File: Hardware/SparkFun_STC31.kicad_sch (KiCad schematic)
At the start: 25 parts, among them J3 Qwiic_RA, J4 I2C, J5 Qwiic_RA, U1 VEML7700-TT

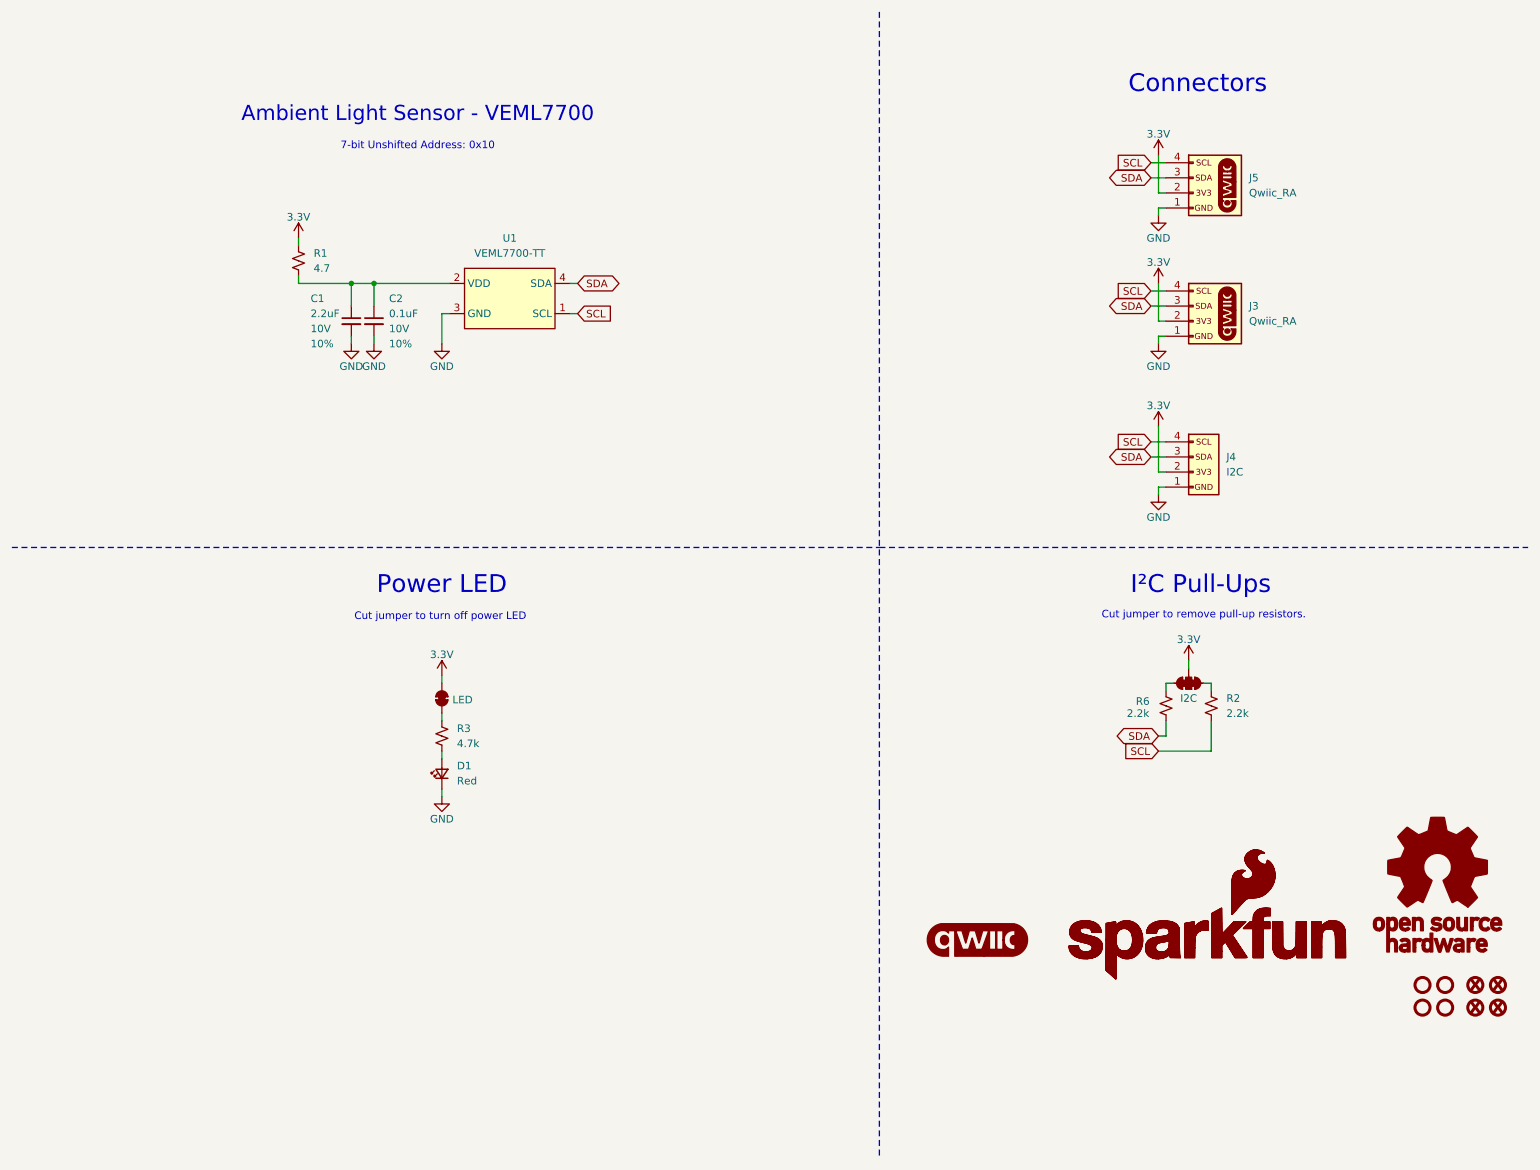
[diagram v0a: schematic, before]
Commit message: Updates the gitignore, finishes the schematic
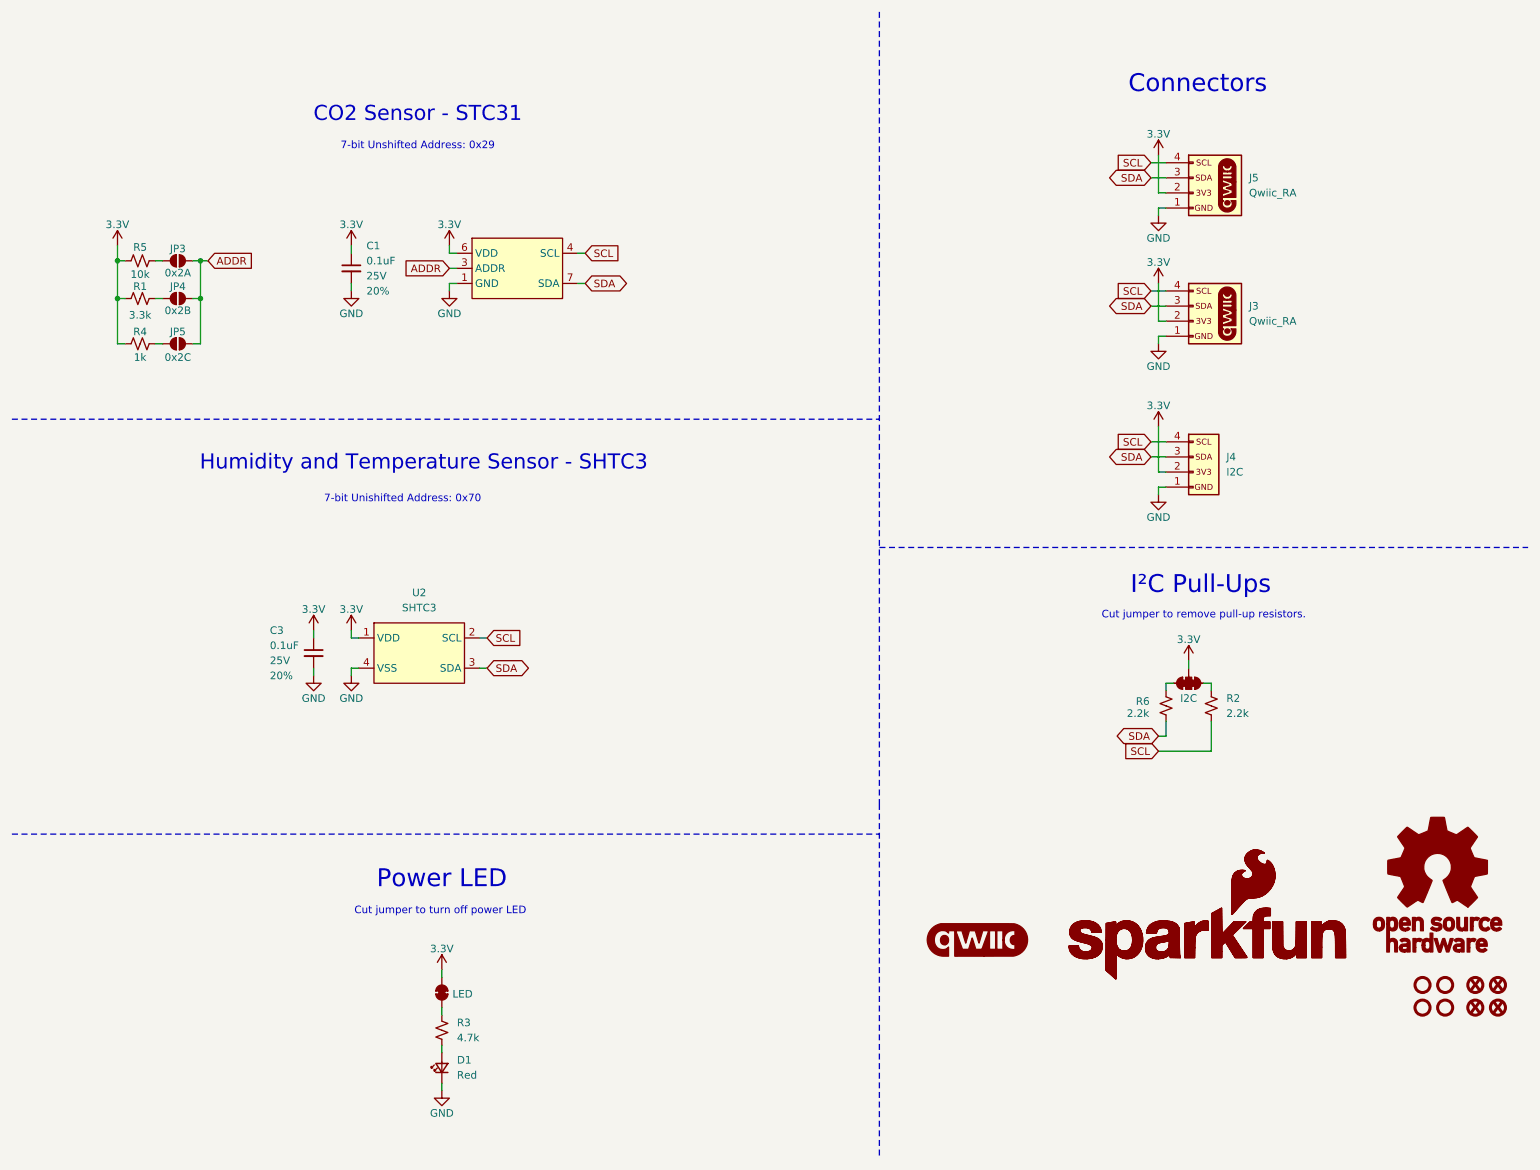
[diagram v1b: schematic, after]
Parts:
- removed C1: 2.2uF, SparkFun-Capacitor:C_0402_1005Metric, symbol SparkFun-Capacitor:2.2uF_0402_10V_10%
- removed C2: 0.1uF, SparkFun-Capacitor:C_0402_1005Metric, symbol SparkFun-Capacitor:0.1uF_0402_10V_10%
- removed R1: 4.7, SparkFun-Resistor:R_0402_1005Metric, symbol SparkFun-Resistor:4.7_0402
- removed U1: VEML7700-TT, SparkFun-Sensor:VEML7700-TT, symbol SparkFun-Sensor:VEML7700-TT
- added C1, C3: 0.1uF, SparkFun-Capacitor:C_0603_1608Metric, symbol SparkFun-Capacitor:0.1uF_0603_25V_20%
- added JP3: 0x2A, SparkFun-Jumper:Jumper_2_NO, symbol SparkFun-Jumper:SolderJumper_2_Open
- added JP4: 0x2B, SparkFun-Jumper:Jumper_2_NO, symbol SparkFun-Jumper:SolderJumper_2_Open
- added JP5: 0x2C, SparkFun-Jumper:Jumper_2_NO, symbol SparkFun-Jumper:SolderJumper_2_Open
- added R1: 3.3k, SparkFun-Resistor:R_0603_1608Metric, symbol SparkFun-Resistor:3.3k_0603
- added R4: 1k, SparkFun-Resistor:R_0603_1608Metric, symbol SparkFun-Resistor:1k_0603
- added R5: 10k, SparkFun-Resistor:R_0603_1608Metric, symbol SparkFun-Resistor:10k_0603
- added U1: STC31, SparkFun-Sensor:STC31, symbol SparkFun-Sensor:STC31
- added U2: SHTC3, SparkFun-Sensor:SHTC3, symbol SparkFun-Sensor:SHTC3
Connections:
- net 3.3V: now also C1.1, C3.1, R1.1, R4.1, R5.1, U1.6 (VDD), U2.1 (VDD)
- net GND: now also C1.2, C3.2, U1.1 (GND), U2.4 (VSS)
- net SCL: now also U1.4 (SCL), U2.2 (SCL)
- net SDA: now also U1.7 (SDA), U2.3 (SDA)
- new net: JP3.1 (A), R5.2
- new net: JP5.1 (A), R4.2
- new net: JP4.1 (A), R1.2
- new net ADDR: JP3.2 (B), JP4.2 (B), JP5.2 (B), U1.3 (ADDR)
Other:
- note added: "7-bit Unishifted Address: 0x70"
- note added: "7-bit Unshifted Address: 0x29"
- note added: "CO2 Sensor - STC31"
- note added: "Humidity and Temperature Sensor - SHTC3"
- note removed: "7-bit Unshifted Address: 0x10"
- note removed: "Ambient Light Sensor - VEML7700"
- moved on the sheet: D1, R3

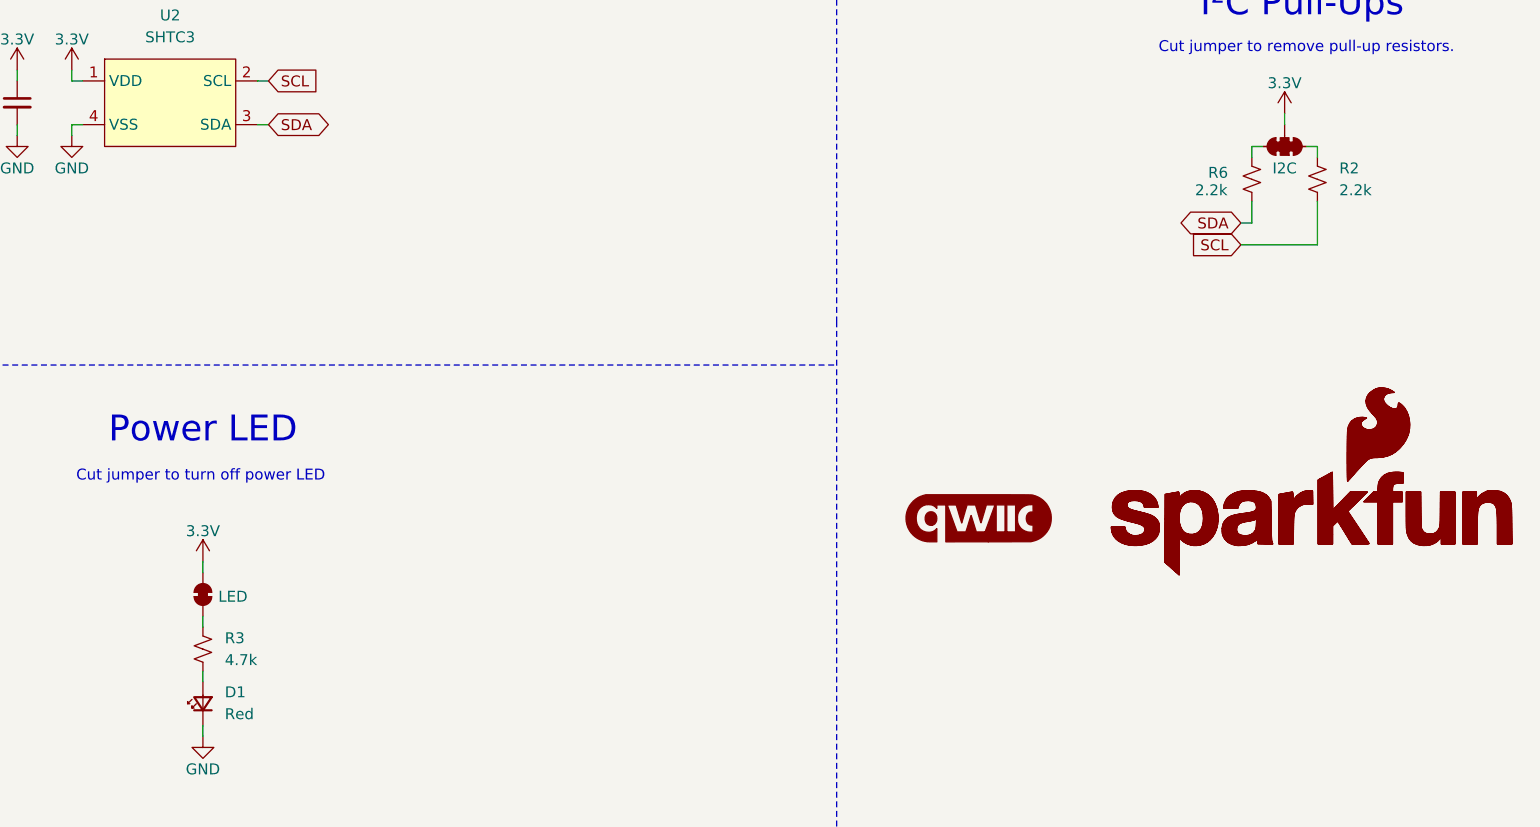
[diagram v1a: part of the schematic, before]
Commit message: Cleans out the PCB
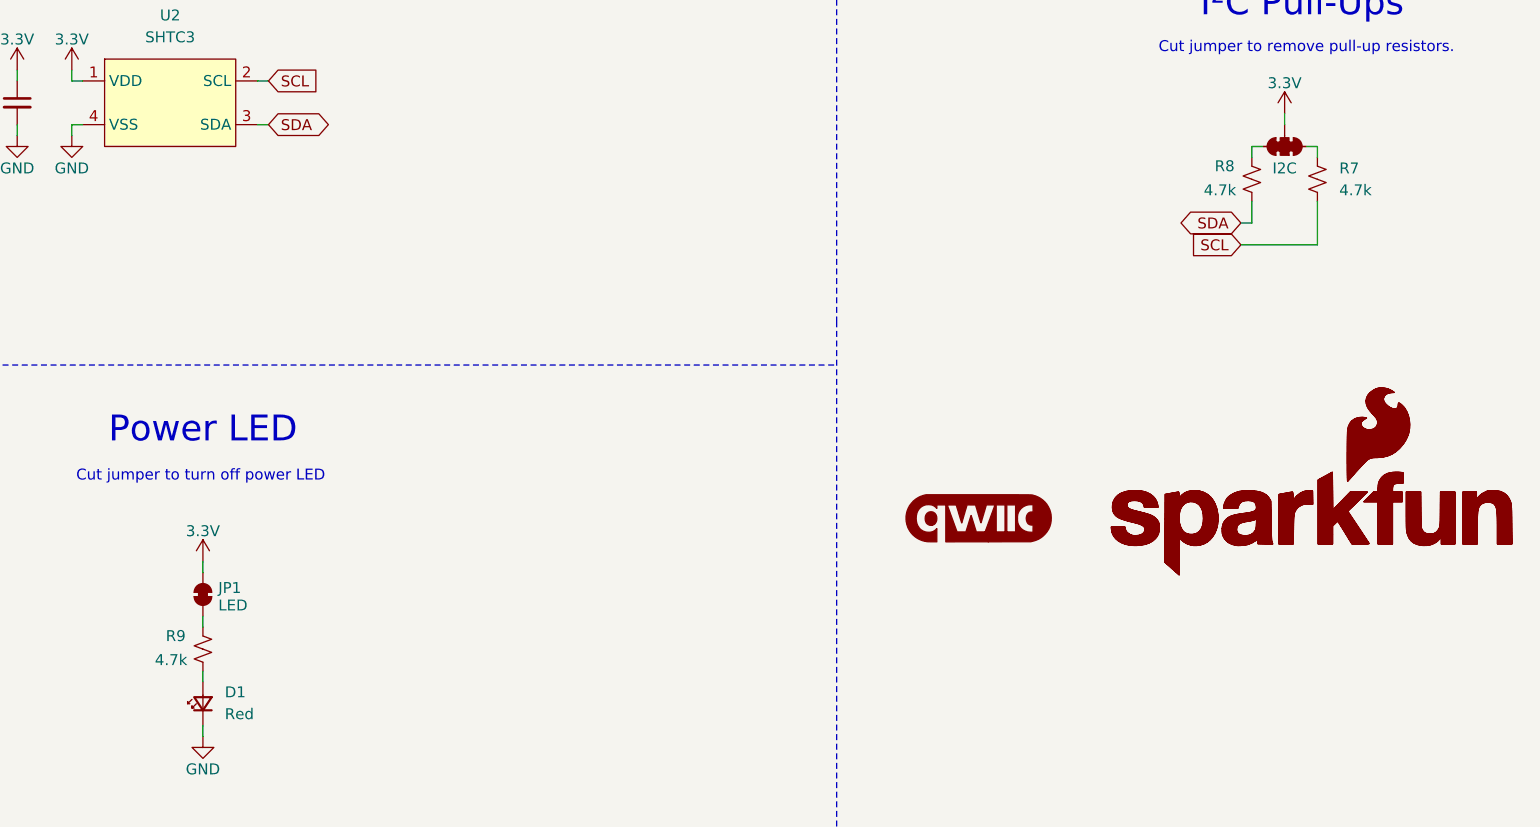
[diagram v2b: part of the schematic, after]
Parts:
- removed R2, R6: 2.2k, SparkFun-Resistor:R_0402_1005Metric, symbol SparkFun-Resistor:2.2k_0402
- removed R3: 4.7k, SparkFun-Resistor:R_0402_1005Metric, symbol SparkFun-Resistor:4.7k_0402
- added R7, R8, R9: 4.7k, SparkFun-Resistor:R_0603_1608Metric, symbol SparkFun-Resistor:4.7k_0603
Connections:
- net SCL: now also R7.1
- net SDA: now also R8.2
- net at D1.2 (A): now also R9.2
- net at JP1.1 (A): now also R9.1
- net at JP2.1 (A): now also R7.2
- net at JP2.3 (C): now also R8.1
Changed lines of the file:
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@@
-	)
-	(symbol
-		(lib_id "SparkFun-Resistor:4.7k_0402")
-		(at 85.09 182.88 90)
-		(unit 1)
-		(exclude_from_sim no)
-		(in_bom yes)
-		(on_board yes)
-		(dnp no)
-		(fields_autoplaced yes)
-		(property "Reference" "R3"
-			(at 87.63 181.6099 90)
-			(effects
-				(font
-					(size 1.27 1.27)
-				)
-				(justify right)
-			)
-		)
-		(property "Value" "4.7k"
-			(at 87.63 184.1499 90)
-			(effects
-				(font
-					(size 1.27 1.27)
-				)
-				(justify right)
-			)
-		)
-		(property "Footprint" "SparkFun-Resistor:R_0402_1005Metric"
-			(at 89.408 182.88 0)
-			(effects
-				(font
-					(size 1.27 1.27)
-				)
-				(hide yes)
-			)
-		)
-		(property "Datasheet" "https://www.vishay.com/docs/20035/dcrcwe3.pdf"
-			(at 93.98 182.88 0)
-			(effects
-				(font
-					(size 1.27 1.27)
-				)
-				(hide yes)
-			)
-		)
-		(property "Description" "Resistor"
-			(at 96.52 182.88 0)
-			(effects
-				(font
-					(size 1.27 1.27)
-				)
-				(hide yes)
-			)
-		)
-		(property "PROD_ID" "RES-15343"
-			(at 91.694 182.88 0)
-			(effects
-				(font
-					(size 1.27 1.27)
-				)
-				(hide yes)
-			)
-		)
-		(pin "2"
-		)
-		(pin "1"
-		)
-		(instances
-			(project ""
-				(path "/e3dd3ae4-244d-4cba-9cca-5d2abf83f29a"
-					(reference "R3")
-					(unit 1)
-				)
-			)
-		)
 	)
 	(symbol
@@
 	)
 	(symbol
+		(lib_id "SparkFun-Resistor:4.7k_0603")
+		(at 207.01 128.27 270)
+		(unit 1)
+		(exclude_from_sim no)
+		(in_bom yes)
+		(on_board yes)
+		(dnp no)
+		(property "Reference" "R8"
+			(at 202.692 126.746 90)
+			(effects
+				(font
+					(size 1.27 1.27)
+				)
+				(justify left)
+			)
+		)
+		(property "Value" "4.7k"
+			(at 201.422 129.54 90)
+			(effects
+				(font
+					(size 1.27 1.27)
+				)
+				(justify left)
+			)
+		)
+		(property "Footprint" "SparkFun-Resistor:R_0603_1608Metric"
+			(at 202.692 128.27 0)
+			(effects
+				(font
+					(size 1.27 1.27)
+				)
+				(hide yes)
+			)
+		)
+		(property "Datasheet" "https://www.vishay.com/docs/20035/dcrcwe3.pdf"
+			(at 198.12 128.27 0)
+			(effects
+				(font
+					(size 1.27 1.27)
+				)
+				(hide yes)
+			)
+		)
+		(property "Description" "Resistor"
+			(at 195.58 128.27 0)
+			(effects
+				(font
+					(size 1.27 1.27)
+				)
+				(hide yes)
+			)
+		)
+		(property "PROD_ID" "RES-07857"
+			(at 200.406 128.27 0)
+			(effects
+				(font
+					(size 1.27 1.27)
+				)
+				(hide yes)
+			)
+		)
+		(pin "2"
+		)
+		(pin "1"
+		)
+		(instances
+			(project ""
+				(path "/e3dd3ae4-244d-4cba-9cca-5d2abf83f29a"
+					(reference "R8")
+					(unit 1)
+				)
+			)
+		)
+	)
+	(symbol
 		(lib_id "SparkFun-Connector:Qwiic_Right_Angle")
 		(at 212.09 39.37 0)
@@
 	)
 	(symbol
-		(lib_id "SparkFun-Resistor:2.2k_0402")
-		(at 214.63 128.27 90)
-		(unit 1)
-		(exclude_from_sim no)
-		(in_bom yes)
-		(on_board yes)
-		(dnp no)
-		(fields_autoplaced yes)
-		(property "Reference" "R2"
-			(at 217.17 126.9999 90)
-			(effects
-				(font
-					(size 1.27 1.27)
-				)
-				(justify right)
-			)
-		)
-		(property "Value" "2.2k"
-			(at 217.17 129.5399 90)
-			(effects
-				(font
-					(size 1.27 1.27)
-				)
-				(justify right)
-			)
-		)
-		(property "Footprint" "SparkFun-Resistor:R_0402_1005Metric"
-			(at 218.948 128.27 0)
-			(effects
-				(font
-					(size 1.27 1.27)
-				)
-				(hide yes)
-			)
-		)
-		(property "Datasheet" "https://www.vishay.com/docs/20035/dcrcwe3.pdf"
-			(at 223.52 128.27 0)
-			(effects
-				(font
-					(size 1.27 1.27)
-				)
-				(hide yes)
-			)
-		)
-		(property "Description" "Resistor"
-			(at 226.06 128.27 0)
-			(effects
-				(font
-					(size 1.27 1.27)
-				)
-				(hide yes)
-			)
-		)
-		(property "PROD_ID" "RES-14341"
-			(at 221.488 128.27 0)
-			(effects
-				(font
-					(size 1.27 1.27)
-				)
-				(hide yes)
-			)
-		)
-		(pin "2"
-		)
-		(pin "1"
-		)
-		(instances
-			(project ""
-				(path "/e3dd3ae4-244d-4cba-9cca-5d2abf83f29a"
-					(reference "R2")
-					(unit 1)
-				)
-			)
-		)
-	)
-	(symbol
 		(lib_id "SparkFun-Hardware:Standoff")
 		(at 254 179.07 0)
@@
 	)
 	(symbol
+		(lib_id "SparkFun-Resistor:4.7k_0603")
+		(at 85.09 182.88 270)
+		(unit 1)
+		(exclude_from_sim no)
+		(in_bom yes)
+		(on_board yes)
+		(dnp no)
+		(property "Reference" "R9"
+			(at 80.772 181.356 90)
+			(effects
+				(font
+					(size 1.27 1.27)
+				)
+				(justify left)
+			)
+		)
+		(property "Value" "4.7k"
+			(at 79.502 184.15 90)
+			(effects
+				(font
+					(size 1.27 1.27)
+				)
+				(justify left)
+			)
+		)
+		(property "Footprint" "SparkFun-Resistor:R_0603_1608Metric"
+			(at 80.772 182.88 0)
+			(effects
+				(font
+					(size 1.27 1.27)
+				)
+				(hide yes)
+			)
+		)
+		(property "Datasheet" "https://www.vishay.com/docs/20035/dcrcwe3.pdf"
+			(at 76.2 182.88 0)
+			(effects
+				(font
+					(size 1.27 1.27)
+				)
+				(hide yes)
+			)
+		)
+		(property "Description" "Resistor"
+			(at 73.66 182.88 0)
+			(effects
+				(font
+					(size 1.27 1.27)
+				)
+				(hide yes)
+			)
+		)
+		(property "PROD_ID" "RES-07857"
+			(at 78.486 182.88 0)
+			(effects
+				(font
+					(size 1.27 1.27)
+				)
+				(hide yes)
+			)
+		)
+		(pin "2"
+		)
+		(pin "1"
+		)
+		(instances
+			(project "SparkFun_STC31"
+				(path "/e3dd3ae4-244d-4cba-9cca-5d2abf83f29a"
+					(reference "R9")
+					(unit 1)
+				)
+			)
+		)
+	)
+	(symbol
 		(lib_id "SparkFun-PowerSymbol:3.3V")
 		(at 85.09 172.72 0)
@@
 		(dnp no)
 		(property "Reference" "JP1"
-			(at 87.63 175.8949 90)
+			(at 86.868 175.768 90)
 			(effects
 				(font
@@
 				)
 				(justify right)
-				(hide yes)
 			)
 		)
 		(property "Value" "LED"
-			(at 86.868 176.784 90)
+			(at 86.868 177.8 90)
 			(effects
 				(font
@@
 	)
 	(symbol
-		(lib_id "SparkFun-Resistor:2.2k_0402")
-		(at 207.01 128.27 270)
-		(unit 1)
-		(exclude_from_sim no)
-		(in_bom yes)
-		(on_board yes)
-		(dnp no)
-		(property "Reference" "R6"
-			(at 201.93 127.508 90)
-			(effects
-				(font
-					(size 1.27 1.27)
-				)
-				(justify left)
-			)
-		)
-		(property "Value" "2.2k"
-			(at 200.406 129.54 90)
-			(effects
-				(font
-					(size 1.27 1.27)
-				)
-				(justify left)
-			)
-		)
-		(property "Footprint" "SparkFun-Resistor:R_0402_1005Metric"
-			(at 202.692 128.27 0)
+		(lib_id "SparkFun-Resistor:4.7k_0603")
+		(at 214.63 128.27 90)
+		(unit 1)
+		(exclude_from_sim no)
+		(in_bom yes)
+		(on_board yes)
+		(dnp no)
+		(fields_autoplaced yes)
+		(property "Reference" "R7"
+			(at 217.17 126.9999 90)
+			(effects
+				(font
+					(size 1.27 1.27)
+				)
+				(justify right)
+			)
+		)
+		(property "Value" "4.7k"
+			(at 217.17 129.5399 90)
+			(effects
+				(font
+					(size 1.27 1.27)
+				)
+				(justify right)
+			)
+		)
+		(property "Footprint" "SparkFun-Resistor:R_0603_1608Metric"
+			(at 218.948 128.27 0)
 			(effects
 				(font
@@
 		)
 		(property "Datasheet" "https://www.vishay.com/docs/20035/dcrcwe3.pdf"
-			(at 198.12 128.27 0)
+			(at 223.52 128.27 0)
 			(effects
 				(font
@@
 		)
 		(property "Description" "Resistor"
-			(at 195.58 128.27 0)
-			(effects
-				(font
-					(size 1.27 1.27)
-				)
-				(hide yes)
-			)
-		)
-		(property "PROD_ID" "RES-14341"
-			(at 200.152 128.27 0)
-			(effects
-				(font
-					(size 1.27 1.27)
-				)
-				(hide yes)
-			)
+			(at 226.06 128.27 0)
+			(effects
+				(font
+					(size 1.27 1.27)
+				)
+				(hide yes)
+			)
+		)
+		(property "PROD_ID" "RES-07857"
+			(at 221.234 128.27 0)
+			(effects
+				(font
+					(size 1.27 1.27)
+				)
+				(hide yes)
+			)
+		)
+		(pin "1"
 		)
 		(pin "2"
 		)
-		(pin "1"
-		)
 		(instances
 			(project ""
 				(path "/e3dd3ae4-244d-4cba-9cca-5d2abf83f29a"
-					(reference "R6")
-					(unit 1)
-				)
+					(reference "R7")
+					(unit 1)
+				)

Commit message: Stacks ground pins for STC31
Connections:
- net GND: now also U1.11 (GND), U1.5 (GND), U1.9 (GND)
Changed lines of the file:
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@@
 		(pin "4"
+		)
+		(pin "5"
+		)
+		(pin "11"
+		)
+		(pin "9"
 		)
 		(instances
